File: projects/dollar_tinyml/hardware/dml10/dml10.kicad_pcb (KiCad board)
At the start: 2 copper layers, 52 x 26 mm, 40 parts, among them J1 Conn_01x03, J2 USB_A, J3 Header 2.54mm, J4 Header 2.54mm, U1 CH32V003F4P6, U2 LTC4054ES5-4.2, U4 LM321, U5 LIS3DH

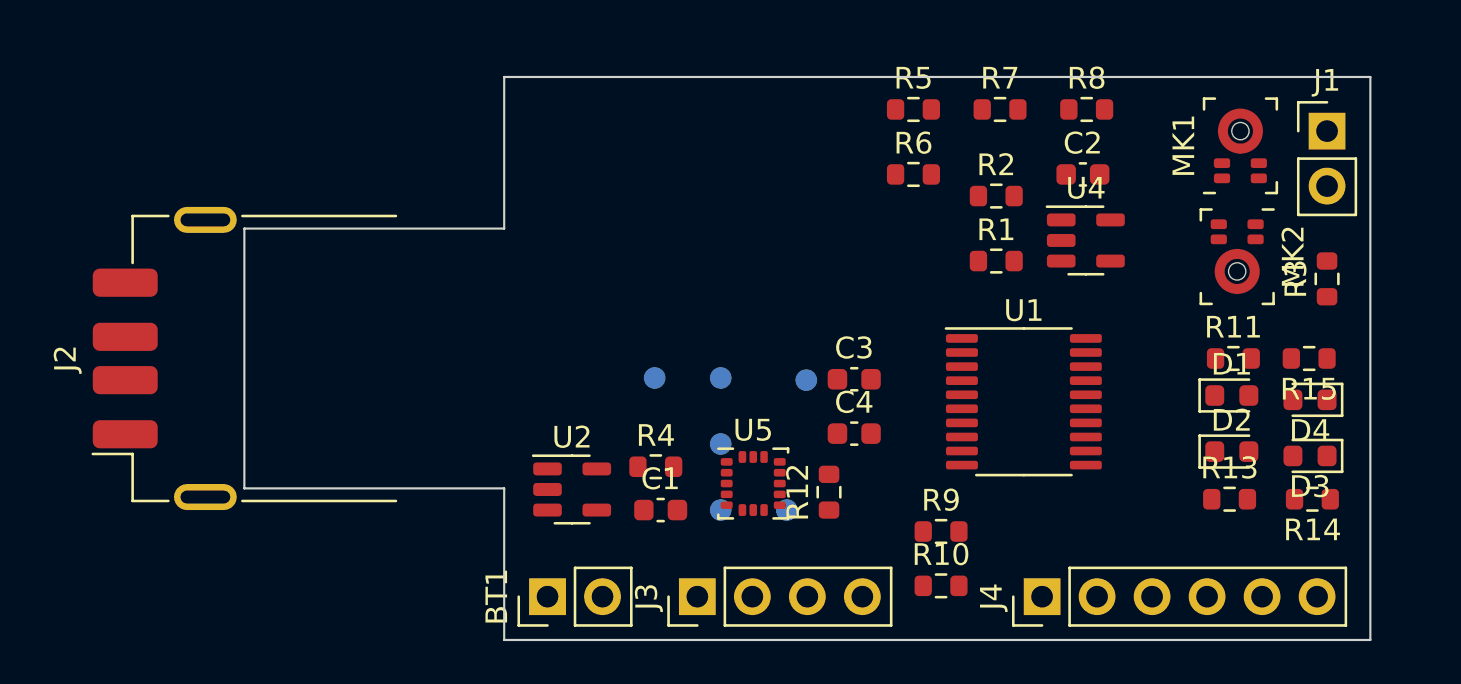
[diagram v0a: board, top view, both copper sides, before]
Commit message: dollarml: Rought footprints and layout in place
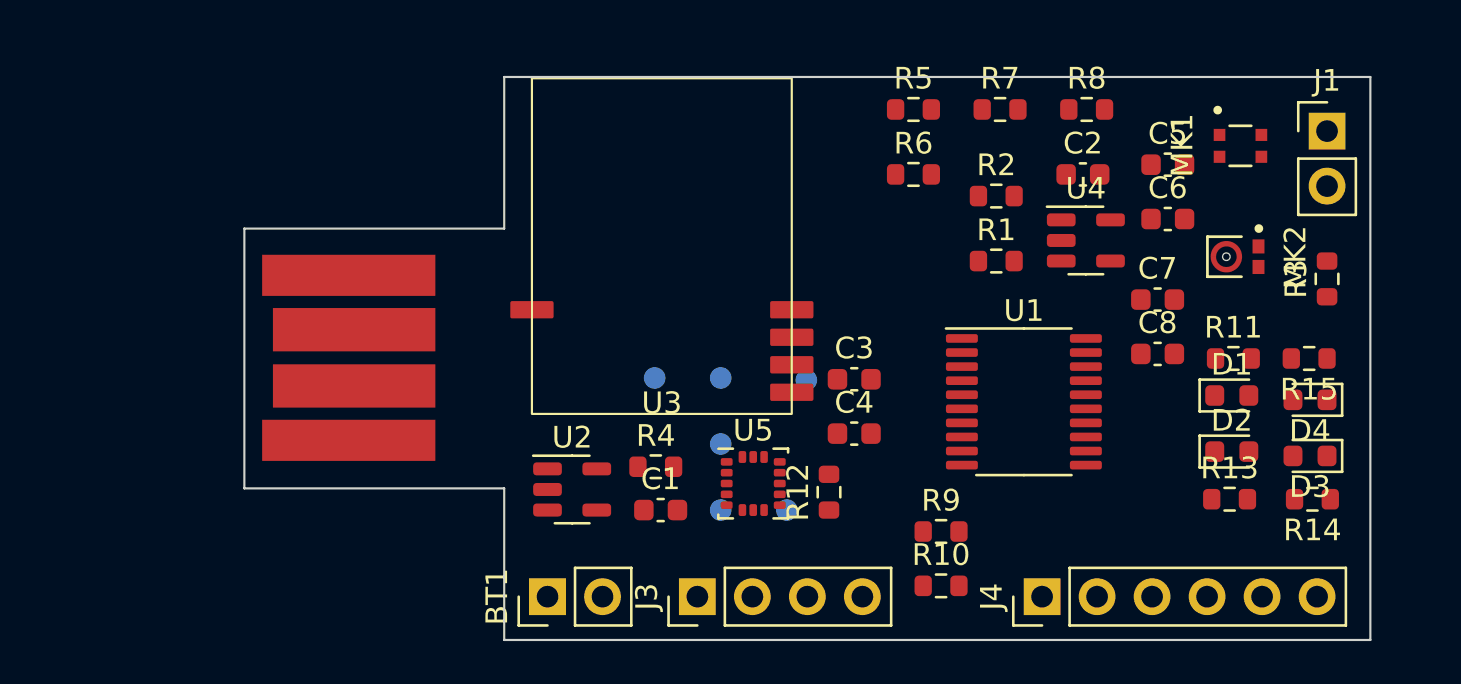
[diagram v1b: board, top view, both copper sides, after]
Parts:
- added C5: 10uF, Capacitor_SMD:C_0603_1608Metric, F.Cu at (70.6, 38.5)
- added C6: 10uF, Capacitor_SMD:C_0603_1608Metric, F.Cu at (70.6, 41.1)
- added C7: 10uF, Capacitor_SMD:C_0603_1608Metric, F.Cu at (70.2, 44.8)
- added C8: 10uF, Capacitor_SMD:C_0603_1608Metric, F.Cu at (70.2, 47.3)
- added U3: BM7161, dml10:BM7161, F.Cu at (47.3, 50.1)
- J2: footprint Connector_USB:USB_A_Receptacle_GCT_USB1046 -> dml10:EdgeUSBTypeA
- MK1: footprint Sensor_Audio:Infineon_PG-LLGA-5-2 -> dml10:XDCR_CMM-2718AT-42308-TR
- MK2: footprint Sensor_Audio:Infineon_PG-LLGA-5-2 -> dml10:XDCR_CMM-2718AB-383161-TR
- moved J2 1.83 mm to (27.9, 47.5), turned to -90 degrees
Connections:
- MK1 pad 1: unconnected-(MK1-OUT+-Pad1) -> /MIC_POWER
- MK1 pad 2: unconnected-(MK1-V_{DD}-Pad2) -> Net-(C5-Pad2)
- MK1 pad 3: unconnected-(MK1-OUT--Pad3) -> Net-(C5-Pad2)
- MK1 pad 4: Net-(MK1-GND-Pad4) -> unconnected-(MK1-OUT-Pad4)
- MK2 pad 1: unconnected-(MK2-OUT+-Pad1) -> /MIC_POWER
- MK2 pad 3: unconnected-(MK2-OUT--Pad3) -> GND

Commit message: dollarml: Some fixes to schematic and layout
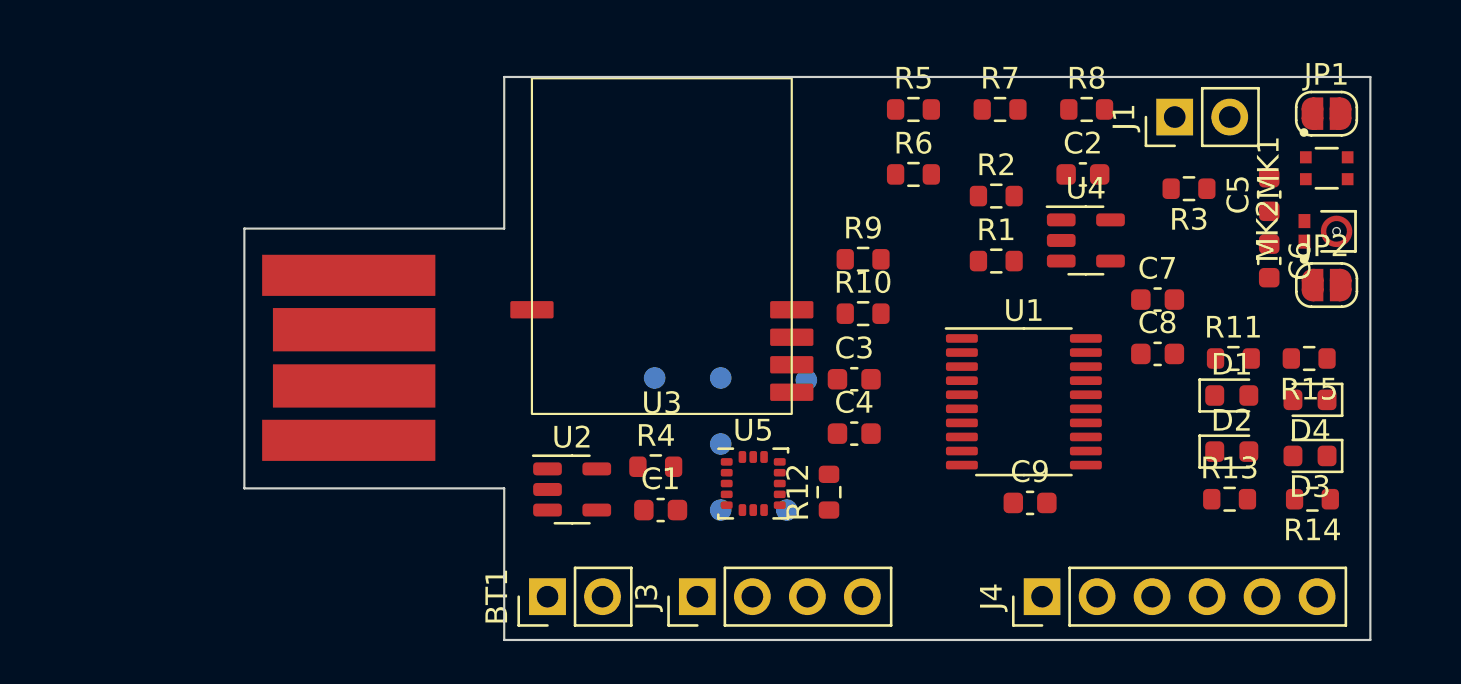
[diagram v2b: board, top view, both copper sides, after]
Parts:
- added C9: 10uF, Capacitor_SMD:C_0603_1608Metric, F.Cu at (64.3, 54.2)
- added JP1: SolderJumper_2_Open, Jumper:SolderJumper-2_P1.3mm_Open_RoundedPad1.0x1.5mm, F.Cu at (78.0, 36.2)
- added JP2: SolderJumper_2_Open, Jumper:SolderJumper-2_P1.3mm_Open_RoundedPad1.0x1.5mm, F.Cu at (78.0, 44.1)
- moved R10 13.1 mm to (56.6, 45.4)
- moved R9 13.1 mm to (56.6, 42.9)
- moved R3 7.61 mm to (71.6, 39.7), turned to 180 degrees
- moved J1 7.06 mm to (71.0, 36.4), turned to 90 degrees
- moved C6 5.07 mm to (75.3, 43.0), turned to -90 degrees
- moved C5 4.88 mm to (75.3, 39.9), turned to 90 degrees
- moved MK2 4.25 mm to (77.9, 41.6), turned to 90 degrees
- moved MK1 4.12 mm to (78.0, 38.7)
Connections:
- C5 pad 2: Net-(C5-Pad2) -> GND
- MK1 pad 2: Net-(C5-Pad2) -> GND
- MK1 pad 3: Net-(C5-Pad2) -> GND
- MK1 pad 4: unconnected-(MK1-OUT-Pad4) -> Net-(JP1-A)
- MK2 pad 2: unconnected-(MK2-OUT-Pad2) -> Net-(JP2-A)

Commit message: dollarml: Do most of layout and routing
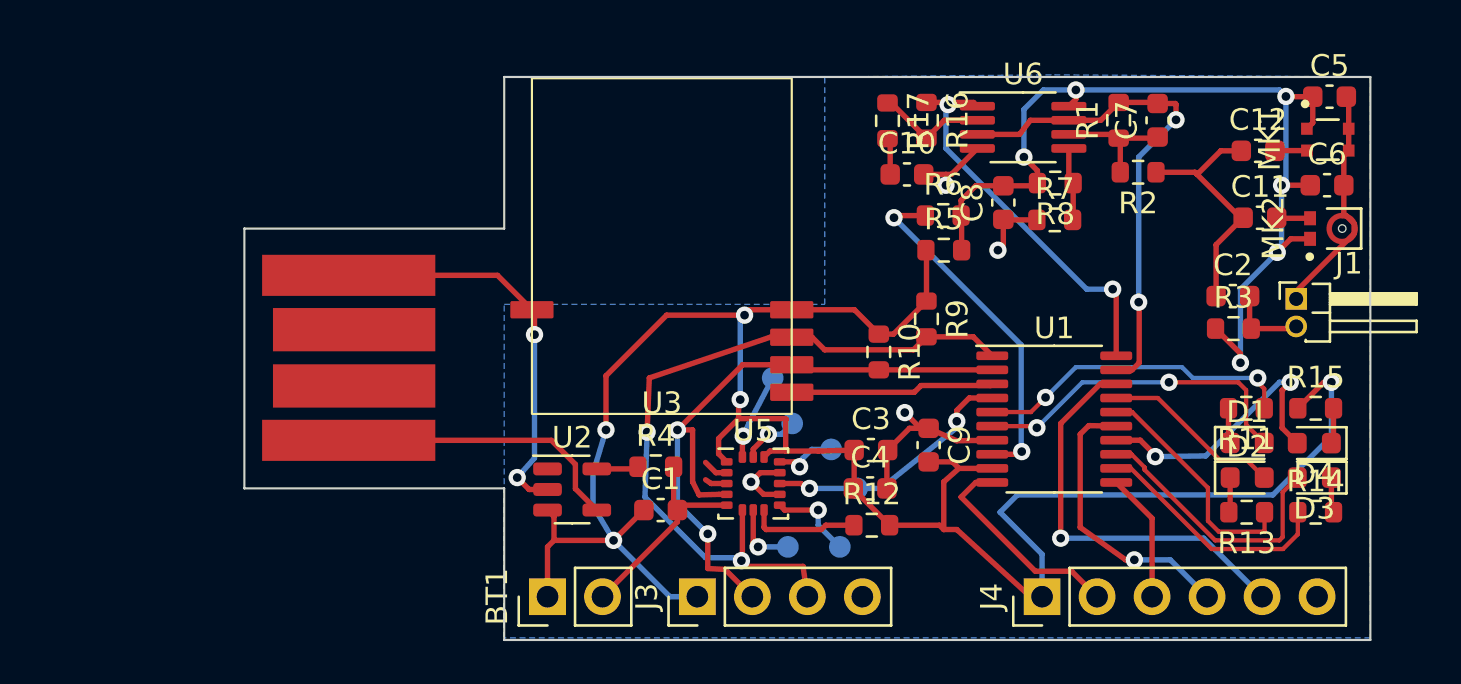
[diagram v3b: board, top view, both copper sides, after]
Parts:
- removed JP1, JP2: SolderJumper_2_Open, Jumper:SolderJumper-2_P1.3mm_Open_RoundedPad1.0x1.5mm
- removed U4: LM321, Package_TO_SOT_SMD:SOT-23-5
- added C10: 10uF, Capacitor_SMD:C_0603_1608Metric, F.Cu at (58.6, 39.0)
- added C11: 10uF, Capacitor_SMD:C_0603_1608Metric, F.Cu at (74.9, 41.0)
- added C12: 10uF, Capacitor_SMD:C_0603_1608Metric, F.Cu at (74.8, 37.9)
- added R16: 68k, Resistor_SMD:R_0603_1608Metric, F.Cu at (59.5, 36.5)
- added R17: 3.3k, Resistor_SMD:R_0603_1608Metric, F.Cu at (57.7, 36.5)
- added U6: LMV358, Package_SO:MSOP-8_3x3mm_P0.65mm, F.Cu at (64.0, 36.8)
- C3: value 10uF -> 100nF
- C7: value 10uF -> 100pF
- J1: footprint Connector_PinHeader_2.54mm:PinHeader_1x02_P2.54mm_Vertical -> Connector_PinHeader_1.27mm:PinHeader_1x02_P1.27mm_Horizontal
- R1: value R -> 68k
- R10, R2, R9: value R -> 3.3k
- R6: value R -> 0ohm
- moved J1 10.1 mm to (76.6, 44.8), turned to 0 degrees
- moved C8 9.98 mm to (63.0, 40.3), turned to 90 degrees
- moved TP7 9.93 mm to (53.1, 56.2)
- moved C2 8.92 mm to (73.7, 44.6)
- moved R1 8.61 mm to (68.4, 36.5), turned to 90 degrees
- moved C7 8.28 mm to (70.2, 36.5), turned to 90 degrees
- moved R3 6.78 mm to (73.7, 46.1), turned to 0 degrees
- moved R5 6.65 mm to (60.3, 42.5)
- moved R2 6.64 mm to (69.3, 38.9), turned to 180 degrees
- moved TP5 6.63 mm to (56.3, 53.5)
- moved TP4 6.07 mm to (55.1, 51.7)
- moved TP6 5.76 mm to (55.5, 56.2)
- moved R7 5.69 mm to (65.4, 41.1)
- moved C9 5.39 mm to (59.6, 51.5), turned to -90 degrees
- moved C5 5.31 mm to (78.1, 35.4), turned to 0 degrees
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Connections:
- C2 pad 1: Net-(C2-Pad1) -> /MIC_INPUT
- C2 pad 2: /MIC_INPUT -> Net-(J1-Pin_2)
- C3 pad 1: /ACC_POWER -> VDD
- C4 pad 1: /ACC_POWER -> VDD
- C7 pad 2: /AUDIO_IN -> /AUDIO_LOW
- J1 pad 2: /MIC_INPUT -> Net-(J1-Pin_2)
- J3 pad 2: /SDA -> /SCL
- J3 pad 3: /SCL -> /SDA
- R1 pad 2: /AUDIO_IN -> /AUDIO_LOW
- R12 pad 2: /ACC_POWER -> VDD
- R15 pad 1: /LED_WHITE_P -> VDD
- R2 pad 1: Net-(C2-Pad1) -> /MIC_INPUT
- R3 pad 2: /MIC_INPUT -> Net-(J1-Pin_2)
- U1 pad 1: unconnected-(U1-PD4-Pad1) -> /SDA
- U1 pad 10: unconnected-(U1-PC0-Pad10) -> /SWDIO
- U1 pad 11: unconnected-(U1-PC1-Pad11) -> /SWCLK
- U1 pad 12: unconnected-(U1-PC2-Pad12) -> /LED_BLUE_P
- U1 pad 13: unconnected-(U1-PC3-Pad13) -> /LED_BLUE_N
- U1 pad 14: unconnected-(U1-PC4-Pad14) -> /LED_WHITE_N
- U1 pad 15: unconnected-(U1-PC5-Pad15) -> /BOOT0
- U1 pad 16: unconnected-(U1-PC6-Pad16) -> /LED_GREEN_P
- U1 pad 17: unconnected-(U1-PC7-Pad17) -> /LED_GREEN_N
- U1 pad 18: unconnected-(U1-PD1-Pad18) -> /RESET
- U1 pad 19: unconnected-(U1-PD2-Pad19) -> /AUDIO_LOW
- U1 pad 2: unconnected-(U1-PD5-Pad2) -> /SCL
- U1 pad 20: unconnected-(U1-PD3-Pad20) -> /AUDIO_HIGH
- U1 pad 3: unconnected-(U1-PD6-Pad3) -> /BLE_INT
- U1 pad 4: unconnected-(U1-PD7-Pad4) -> /ACC_INT1
- U1 pad 5: unconnected-(U1-PA1-Pad5) -> /LED_RED_P
- U1 pad 6: unconnected-(U1-PA2-Pad6) -> /LED_RED_N
- U1 pad 8: unconnected-(U1-PD0-Pad8) -> /MIC_POWER_CTRL
- U5 pad 1: /ACC_POWER -> VDD
- U5 pad 14: /ACC_POWER -> VDD
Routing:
- net VDD: track 0.00 -> 101.7 mm, vias 0 -> 5
- net GND: track 0.00 -> 57.8 mm, vias 0 -> 6
- net /MIC_POWER: track 0.00 -> 44.5 mm, vias 0 -> 6
- net /SDA: track 0.00 -> 35.1 mm, vias 0 -> 2
- net /SCL: track 0.00 -> 30.5 mm, vias 0 -> 2
- net /AUDIO_LOW: track 0.00 -> 23.7 mm, vias 0 -> 2
- net /RESET: track 0.00 -> 19.1 mm, vias 0 -> 1
- net /AUDIO_HIGH: track 0.00 -> 18.0 mm, vias 0 -> 2
- net /MIC_POWER_CTRL: track 0.00 -> 16.3 mm, vias 0 -> 2
- net /LED_RED_N: track 0.00 -> 15.6 mm, vias 0 -> 2
- net /LED_RED_P: track 0.00 -> 14.5 mm, vias 0 -> 2
- net VBUS: track 0.00 -> 13.4 mm
- net /BOOT0: track 0.00 -> 13.2 mm, vias 0 -> 1
- net /LED_WHITE_N: track 0.00 -> 13.1 mm, vias 0 -> 2
- net /LED_BLUE_N: track 0.00 -> 12.5 mm
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- added copper zone on B.Cu, net GND
